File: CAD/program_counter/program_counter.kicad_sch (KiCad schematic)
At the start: 54 parts, among them J1 Conn_01x18_Pin, J2 Conn_01x06_Pin, SW1 SW_Push, SW2 SW_Push, U1 74HC161, U2 74HC161, U3 74HC161, U4 74HC161, U5 74HC245, U6 74HC245, U7 74HC165, U8 74HC165, U9 ATmega328P-A, Y1 16MHz

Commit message: update PC, move crystal, change capacitors, add testpoints
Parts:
- added TP5, TP6, TP7: TestPoint, TestPoint:TestPoint_THTPad_D1.0mm_Drill0.5mm, symbol Connector:TestPoint
- C1, C12, C13, C2, C3, C4, C5, C6, C7, C8: LCSC (none) -> C28233
- C10, C11: value 22pF -> 12pF; LCSC (none) -> C1792
- C9: LCSC (none) -> C15850
- D17, D19: LCSC (none) -> C2297
- D18, D20: LCSC (none) -> C2296
- D21: LCSC (none) -> C84256
- DS1, J2, TP1, TP2, TP3, TP4: now left out of the parts list
- J1: LCSC (none) -> C2894989
- R17, R18, R19, R20, R21: LCSC (none) -> C17513
- R22, R23, R24: LCSC (none) -> C17414
- SW1, SW2: Details (none) -> https://jlcpcb.com/partdetail/XKBConnection-TS_1187A_B_AB/C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; LCSC (none) -> C318884
- U9: Details (none) -> https://jlcpcb.com/partdetail/MicrochipTech-ATMEGA328PAU/C1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; LCSC (none) -> C14877
- Y1: Details (none) -> https://jlcpcb.com/partdetail/YXC_CrystalOscillators-X32251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; LCSC (none) -> C13738
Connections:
- net GND: now also TP7.1
- net xtal1: now reaches C11.1, U9.7 (XTAL1/PB6), Y1.3
- net xtal1: now also TP6.1
- net xtal2: now reaches C10.1, U9.8 (XTAL2/PB7), Y1.1
- net xtal2: now also TP5.1

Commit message: update KiCAD version 10.0
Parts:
- added R8: 10k, Resistor_SMD:R_0805_2012Metric, symbol Device:R
- renumbered D17 to D1, D18 to D2, D19 to D3, D20 to D4, D21 to D5, R17 to R1, R18 to R2, R19 to R3, R20 to R4, R21 to R5, R22 to R6, R23 to R7, R24 to R9
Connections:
- net +5V: now also R8.1
- net CS: now also R8.2

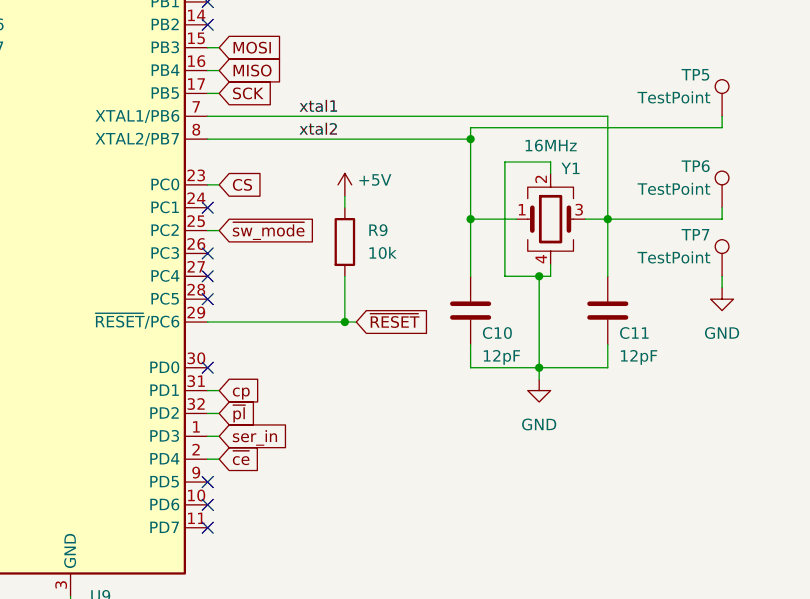
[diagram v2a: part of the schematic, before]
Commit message: exclude known warnings in ERC and DRC
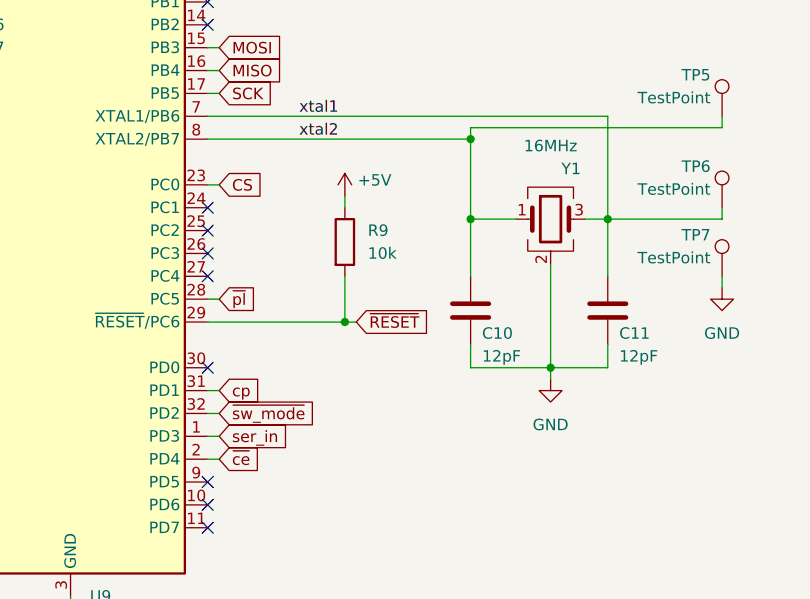
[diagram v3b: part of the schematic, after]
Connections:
- net ~{pl}: now also U9.28 (PC5); no longer U9.32 (PD2)
- net ~{sw_mode}: now also U9.32 (PD2); no longer U9.25 (PC2)
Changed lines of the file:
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@@
 	)
 	(junction
-		(at 372.11 146.05)
-		(diameter 0)
-		(color 0 0 0 0)
-	)
-	(junction
 		(at 71.12 140.97)
 		(diameter 0)
@@
 	)
 	(junction
-		(at 372.11 135.89)
-		(diameter 0)
-		(color 0 0 0 0)
-	)
-	(junction
 		(at 83.82 133.35)
 		(diameter 0)
@@
 	)
 	(junction
+		(at 373.38 146.05)
+		(diameter 0)
+		(color 0 0 0 0)
+	)
+	(junction
 		(at 58.42 133.35)
 		(diameter 0)
@@
 	)
 	(no_connect
-		(at 335.28 138.43)
+		(at 335.28 130.81)
 	)
 	(no_connect
@@
 	(wire
 		(pts
-			(xy 372.11 146.05) (xy 372.11 147.32)
+			(xy 373.38 146.05) (xy 373.38 147.32)
 		)
 		(stroke
@@
 	(wire
 		(pts
-			(xy 364.49 146.05) (xy 372.11 146.05)
+			(xy 364.49 146.05) (xy 373.38 146.05)
 		)
 		(stroke
@@
 	(wire
 		(pts
+			(xy 336.55 138.43) (xy 335.28 138.43)
+		)
+		(stroke
+			(width 0)
+			(type default)
+		)
+	)
+	(wire
+		(pts
 			(xy 46.99 60.96) (xy 46.99 62.23)
 		)
@@
 	(wire
 		(pts
+			(xy 373.38 146.05) (xy 379.73 146.05)
+		)
+		(stroke
+			(width 0)
+			(type default)
+		)
+	)
+	(wire
+		(pts
 			(xy 134.62 99.06) (xy 147.32 99.06)
 		)
@@
 	(wire
 		(pts
-			(xy 372.11 135.89) (xy 373.38 135.89)
-		)
-		(stroke
-			(width 0)
-			(type default)
-		)
-	)
-	(wire
-		(pts
 			(xy 241.3 147.32) (xy 241.3 148.59)
 		)
@@
 	(wire
 		(pts
-			(xy 368.3 123.19) (xy 368.3 135.89)
-		)
-		(stroke
-			(width 0)
-			(type default)
-		)
-	)
-	(wire
-		(pts
 			(xy 322.58 212.09) (xy 330.2 212.09)
 		)
@@
 	(wire
 		(pts
-			(xy 373.38 123.19) (xy 368.3 123.19)
-		)
-		(stroke
-			(width 0)
-			(type default)
-		)
-	)
-	(wire
-		(pts
 			(xy 392.43 118.11) (xy 392.43 119.38)
 		)
@@
 	(wire
 		(pts
-			(xy 372.11 135.89) (xy 372.11 146.05)
+			(xy 373.38 134.62) (xy 373.38 146.05)
 		)
 		(stroke
@@
 	(wire
 		(pts
-			(xy 373.38 123.19) (xy 373.38 124.46)
-		)
-		(stroke
-			(width 0)
-			(type default)
-		)
-	)
-	(wire
-		(pts
 			(xy 320.04 92.71) (xy 322.58 92.71)
 		)
@@
 	(wire
 		(pts
-			(xy 336.55 130.81) (xy 335.28 130.81)
-		)
-		(stroke
-			(width 0)
-			(type default)
-		)
-	)
-	(wire
-		(pts
 			(xy 320.04 90.17) (xy 320.04 92.71)
 		)
@@
 		)
 	)
-	(wire
-		(pts
-			(xy 373.38 135.89) (xy 373.38 134.62)
-		)
-		(stroke
-			(width 0)
-			(type default)
-		)
-	)
 	(bus
 		(pts
@@
 	(wire
 		(pts
-			(xy 372.11 146.05) (xy 379.73 146.05)
-		)
-		(stroke
-			(width 0)
-			(type default)
-		)
-	)
-	(wire
-		(pts
 			(xy 364.49 143.51) (xy 364.49 146.05)
 		)
@@
 	(wire
 		(pts
-			(xy 368.3 135.89) (xy 372.11 135.89)
-		)
-		(stroke
-			(width 0)
-			(type default)
-		)
-	)
-	(wire
-		(pts
 			(xy 133.35 30.48) (xy 147.32 30.48)
 		)
@@
 		)
 	)
+	(global_label "~{pl}"
+		(shape input)
+		(at 336.55 138.43 0)
+		(fields_autoplaced yes)
+		(effects
+			(font
+				(size 1.27 1.27)
+			)
+			(justify left)
+		)
+		(property "Intersheetrefs" "${INTERSHEET_REFS}"
+			(at 341.3494 138.43 0)
+			(hide yes)
+			(show_name no)
+			(do_not_autoplace no)
+			(effects
+				(font
+					(size 1.27 1.27)
+				)
+				(justify left)
+			)
+		)
+	)
 	(global_label "MOSI"
 		(shape input)
@@
 		)
 	)
-	(global_label "~{sw_mode}"
-		(shape input)
-		(at 336.55 130.81 0)
-		(fields_autoplaced yes)
-		(effects
-			(font
-				(size 1.27 1.27)
-			)
-			(justify left)
-		)
-		(property "Intersheetrefs" "${INTERSHEET_REFS}"
-			(at 347.9413 130.81 0)
-			(hide yes)
-			(show_name no)
-			(do_not_autoplace no)
-			(effects
-				(font
-					(size 1.27 1.27)
-				)
-				(justify left)
-			)
-		)
-	)
 	(global_label "~{rst}"
 		(shape input)
@@
 		)
 	)
+	(global_label "~{sw_mode}"
+		(shape input)
+		(at 336.55 151.13 0)
+		(fields_autoplaced yes)
+		(effects
+			(font
+				(size 1.27 1.27)
+			)
+			(justify left)
+		)
+		(property "Intersheetrefs" "${INTERSHEET_REFS}"
+			(at 347.9413 151.13 0)
+			(hide yes)
+			(show_name no)
+			(do_not_autoplace no)
+			(effects
+				(font
+					(size 1.27 1.27)
+				)
+				(justify left)
+			)
+		)
+	)
 	(global_label "~{pc_L_out}"
 		(shape input)
@@
 		)
 	)
-	(global_label "~{pl}"
-		(shape input)
-		(at 336.55 151.13 0)
-		(fields_autoplaced yes)
-		(effects
-			(font
-				(size 1.27 1.27)
-			)
-			(justify left)
-		)
-		(property "Intersheetrefs" "${INTERSHEET_REFS}"
-			(at 341.3494 151.13 0)
-			(hide yes)
-			(show_name no)
-			(do_not_autoplace no)
-			(effects
-				(font
-					(size 1.27 1.27)
-				)
-				(justify left)
-			)
-		)
-	)
 	(symbol
 		(lib_id "8bit_computer:74HC245")
@@
 	(symbol
 		(lib_id "power:GND")
-		(at 372.11 147.32 0)
+		(at 373.38 147.32 0)
 		(unit 1)
 		(body_style 1)
@@
 		(fields_autoplaced yes)
 		(property "Reference" "#PWR024"
-			(at 372.11 153.67 0)
+			(at 373.38 153.67 0)
 			(hide yes)
 			(show_name no)
@@
 		)
 		(property "Value" "GND"
-			(at 372.11 152.4 0)
+			(at 373.38 152.4 0)
 			(show_name no)
 			(do_not_autoplace no)
@@
 		)
 		(property "Footprint" ""
-			(at 372.11 147.32 0)
+			(at 373.38 147.32 0)
 			(hide yes)
 			(show_name no)
@@
 		)
 		(property "Datasheet" ""
-			(at 372.11 147.32 0)
+			(at 373.38 147.32 0)
 			(hide yes)
 			(show_name no)
@@
 		)
 		(property "Description" "Power symbol creates a global label with name \"GND\" , ground"
-			(at 372.11 147.32 0)
+			(at 373.38 147.32 0)
 			(hide yes)
 			(show_name no)
@@
 			)
 		)
-		(property "Description" "-40℃~+85℃ 16MHz 9pF Crystal Oscillator ±10ppm ±20ppm SMD3225-4P Crystals ROHS"
+		(property "Description" "Four pin crystal, GND on pins 2 and 4"
 			(at 373.38 129.54 0)
 			(hide yes)
